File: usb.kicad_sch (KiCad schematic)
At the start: 4 parts, among them J3 TYPE-C-31-M-12

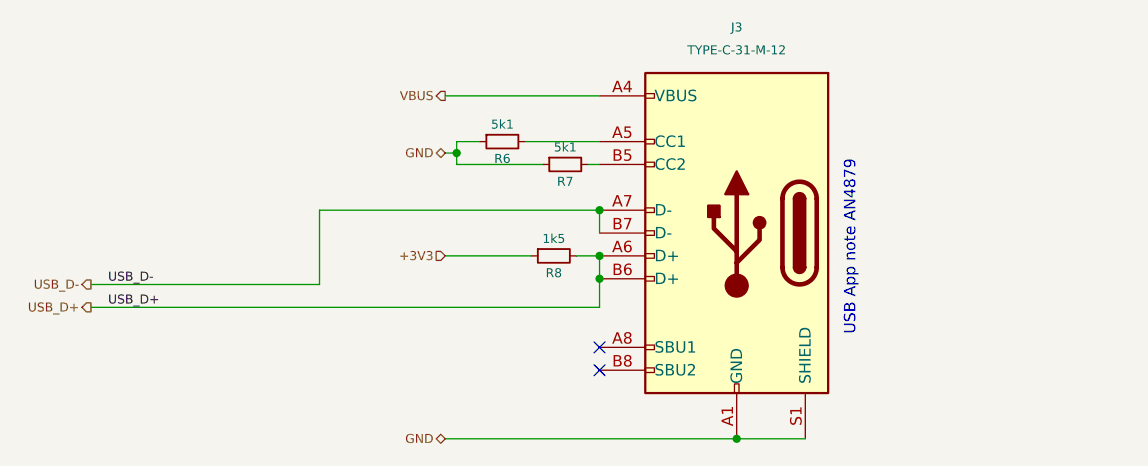
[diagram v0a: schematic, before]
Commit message: Finish schematic with all pins
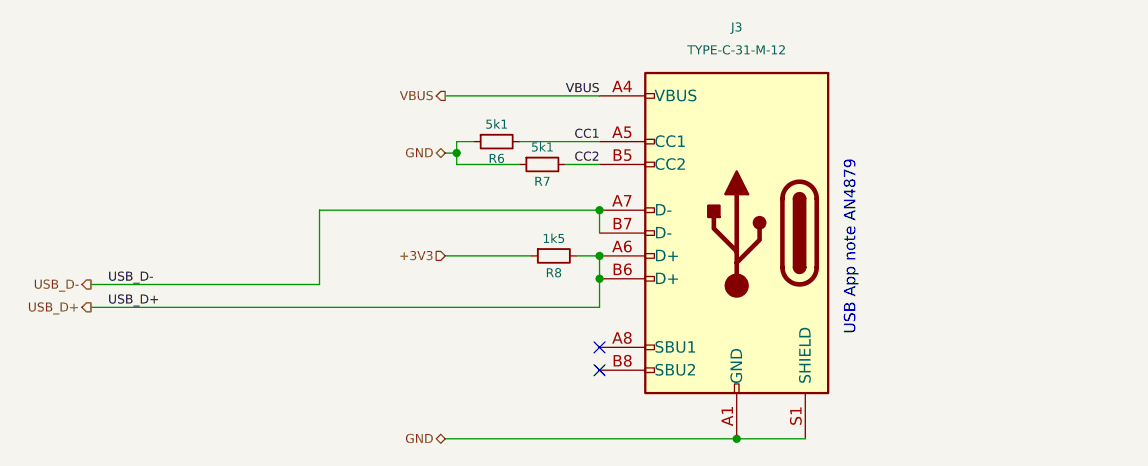
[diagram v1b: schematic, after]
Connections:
- net CC1: now reaches J3.A5 (CC1), R6.2
- net CC2: now reaches J3.B5 (CC2), R7.2
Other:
- moved on the sheet: R6, R7
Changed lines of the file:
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@@
   (no_connect (at 102.235 62.865))
   (no_connect (at 102.235 65.405))
-  (wire (pts (xy 95.885 42.545) (xy 86.36 42.545))
+  (wire (pts (xy 93.345 42.545) (xy 86.36 42.545))
     (stroke (width 0) (type default))
   )
@@
     (stroke (width 0) (type default))
   )
-  (wire (pts (xy 102.235 42.545) (xy 100.965 42.545))
+  (wire (pts (xy 102.235 42.545) (xy 98.425 42.545))
     (stroke (width 0) (type default))
   )
@@
     (stroke (width 0) (type default))
   )
-  (wire (pts (xy 102.235 40.005) (xy 93.98 40.005))
+  (wire (pts (xy 102.235 40.005) (xy 93.345 40.005))
     (stroke (width 0) (type default))
   )
@@
     (stroke (width 0) (type default))
   )
-  (wire (pts (xy 88.9 40.005) (xy 86.36 40.005))
+  (wire (pts (xy 88.265 40.005) (xy 86.36 40.005))
     (stroke (width 0) (type default))
   )
@@
     (effects (font (size 1.27 1.27)) (justify left bottom))
   )
+  (label "VBUS" (at 102.235 34.925 180) (fields_autoplaced)
+    (effects (font (size 1 1)) (justify right bottom))
+  )
   (label "USB_D-" (at 47.625 55.88 0) (fields_autoplaced)
     (effects (font (size 1 1)) (justify left bottom))
@@
     (effects (font (size 1 1)) (justify left bottom))
   )
+  (label "CC2" (at 102.235 42.545 180) (fields_autoplaced)
+    (effects (font (size 1 1)) (justify right bottom))
+  )
+  (label "CC1" (at 102.235 40.005 180) (fields_autoplaced)
+    (effects (font (size 1 1)) (justify right bottom))
+  )
   (hierarchical_label "USB_D-" (shape output) (at 45.72 55.88 180) (fields_autoplaced)
     (effects (font (size 1 1)) (justify right))
@@
     (effects (font (size 1 1)) (justify right))
   )
-  (symbol (lib_id "Device:R_Small") (at 91.44 40.005 90) (mirror x) (unit 1)
+  (symbol (lib_id "Device:R_Small") (at 90.805 40.005 90) (mirror x) (unit 1)
     (in_bom yes) (on_board yes) (dnp no)
-    (property "Reference" "R6" (at 91.44 41.91 90)
-      (effects (font (size 1 1)))
-    )
-    (property "Value" "5k1" (at 91.44 38.1 90)
-      (effects (font (size 1 1)))
-    )
-    (property "Footprint" "Resistor_SMD:R_0402_1005Metric" (at 91.44 40.005 0)
-      (effects (font (size 1 1)) hide)
-    )
-    (property "Datasheet" "~" (at 91.44 40.005 0)
-      (effects (font (size 1 1)) hide)
-    )
-    (property "Description" "62.5mW Thick Film Resistors ±100ppm/℃ ±1% 5.1kΩ 0402  Chip Resistor - Surface Mount ROHS" (at 91.44 40.005 0)
-      (effects (font (size 1 1)) hide)
-    )
-    (property "JLCPCB Part #" "C25905" (at 91.44 40.005 0)
-      (effects (font (size 1 1)) hide)
-    )
-    (property "Manufacturer" "UNI-ROYAL(Uniroyal Elec)" (at 91.44 40.005 0)
-      (effects (font (size 1 1)) hide)
-    )
-    (property "Manufacturer_Part_Number" "0402WGF5101TCE" (at 91.44 40.005 0)
-      (effects (font (size 1 1)) hide)
-    )
-    (property "Partnumber" "0402WGF5101TCE" (at 91.44 40.005 0)
-      (effects (font (size 1 1)) hide)
-    )
-    (property "Manufacturer_Name" "UNI-ROYAL(Uniroyal Elec)" (at 91.44 40.005 0)
-      (effects (font (size 1 1)) hide)
-    )
-    (property "isBasicPart" "YES" (at 91.44 40.005 0)
+    (property "Reference" "R6" (at 90.805 41.91 90)
+      (effects (font (size 1 1)))
+    )
+    (property "Value" "5k1" (at 90.805 38.1 90)
+      (effects (font (size 1 1)))
+    )
+    (property "Footprint" "Resistor_SMD:R_0402_1005Metric" (at 90.805 40.005 0)
+      (effects (font (size 1 1)) hide)
+    )
+    (property "Datasheet" "~" (at 90.805 40.005 0)
+      (effects (font (size 1 1)) hide)
+    )
+    (property "Description" "62.5mW Thick Film Resistors ±100ppm/℃ ±1% 5.1kΩ 0402  Chip Resistor - Surface Mount ROHS" (at 90.805 40.005 0)
+      (effects (font (size 1 1)) hide)
+    )
+    (property "JLCPCB Part #" "C25905" (at 90.805 40.005 0)
+      (effects (font (size 1 1)) hide)
+    )
+    (property "Manufacturer" "UNI-ROYAL(Uniroyal Elec)" (at 90.805 40.005 0)
+      (effects (font (size 1 1)) hide)
+    )
+    (property "Manufacturer_Part_Number" "0402WGF5101TCE" (at 90.805 40.005 0)
+      (effects (font (size 1 1)) hide)
+    )
+    (property "Partnumber" "0402WGF5101TCE" (at 90.805 40.005 0)
+      (effects (font (size 1 1)) hide)
+    )
+    (property "Manufacturer_Name" "UNI-ROYAL(Uniroyal Elec)" (at 90.805 40.005 0)
+      (effects (font (size 1 1)) hide)
+    )
+    (property "isBasicPart" "YES" (at 90.805 40.005 0)
       (effects (font (size 1 1)) hide)
     )
@@
     )
   )
-  (symbol (lib_id "Device:R_Small") (at 98.425 42.545 90) (mirror x) (unit 1)
+  (symbol (lib_id "Device:R_Small") (at 95.885 42.545 90) (mirror x) (unit 1)
     (in_bom yes) (on_board yes) (dnp no)
-    (property "Reference" "R7" (at 98.425 44.45 90)
-      (effects (font (size 1 1)))
-    )
-    (property "Value" "5k1" (at 98.425 40.64 90)
-      (effects (font (size 1 1)))
-    )
-    (property "Footprint" "Resistor_SMD:R_0402_1005Metric" (at 98.425 42.545 0)
-      (effects (font (size 1 1)) hide)
-    )
-    (property "Datasheet" "~" (at 98.425 42.545 0)
-      (effects (font (size 1 1)) hide)
-    )
-    (property "Description" "62.5mW Thick Film Resistors ±100ppm/℃ ±1% 5.1kΩ 0402  Chip Resistor - Surface Mount ROHS" (at 98.425 42.545 0)
-      (effects (font (size 1 1)) hide)
-    )
-    (property "JLCPCB Part #" "C25905" (at 98.425 42.545 0)
-      (effects (font (size 1 1)) hide)
-    )
-    (property "Manufacturer" "UNI-ROYAL(Uniroyal Elec)" (at 98.425 42.545 0)
-      (effects (font (size 1 1)) hide)
-    )
-    (property "Manufacturer_Part_Number" "0402WGF5101TCE" (at 98.425 42.545 0)
-      (effects (font (size 1 1)) hide)
-    )
-    (property "Partnumber" "0402WGF5101TCE" (at 98.425 42.545 0)
-      (effects (font (size 1 1)) hide)
-    )
-    (property "Manufacturer_Name" "UNI-ROYAL(Uniroyal Elec)" (at 98.425 42.545 0)
-      (effects (font (size 1 1)) hide)
-    )
-    (property "isBasicPart" "YES" (at 98.425 42.545 0)
-      (effects (font (size 1 1)) hide)
-    )
+    (property "Reference" "R7" (at 95.885 44.45 90)
+      (effects (font (size 1 1)))
+    )
+    (property "Value" "5k1" (at 95.885 40.64 90)
+      (effects (font (size 1 1)))
+    )
+    (property "Footprint" "Resistor_SMD:R_0402_1005Metric" (at 95.885 42.545 0)
+      (effects (font (size 1 1)) hide)
+    )
+    (property "Datasheet" "~" (at 95.885 42.545 0)
+      (effects (font (size 1 1)) hide)
+    )
+    (property "Description" "62.5mW Thick Film Resistors ±100ppm/℃ ±1% 5.1kΩ 0402  Chip Resistor - Surface Mount ROHS" (at 95.885 42.545 0)
+      (effects (font (size 1 1)) hide)
+    )
+    (property "JLCPCB Part #" "C25905" (at 95.885 42.545 0)
+      (effects (font (size 1 1)) hide)
+    )
+    (property "Manufacturer" "UNI-ROYAL(Uniroyal Elec)" (at 95.885 42.545 0)
+      (effects (font (size 1 1)) hide)
+    )
+    (property "Manufacturer_Part_Number" "0402WGF5101TCE" (at 95.885 42.545 0)
+      (effects (font (size 1 1)) hide)
+    )
+    (property "Partnumber" "0402WGF5101TCE" (at 95.885 42.545 0)
+      (effects (font (size 1 1)) hide)
+    )
+    (property "Manufacturer_Name" "UNI-ROYAL(Uniroyal Elec)" (at 95.885 42.545 0)
+      (effects (font (size 1 1)) hide)
+    )
+    (property "isBasicPart" "YES" (at 95.885 42.545 0)
+      (effects (font (size 1 1)) hide)
+    )

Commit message: WIP
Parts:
- removed J3: TYPE-C-31-M-12, Connector_USB:USB_C_Receptacle_HRO_TYPE-C-31-M-12, symbol Project_Library:USB_C_Receptacle_USB2.0
- added J2: SHOU HAN TYPE-C 16PIN 2MD(073) (C2765186), Project_Library:SHOU HAN TYPE-C 16PIN 2MD(073) (C2765186), symbol Project_Library:SHOU HAN TYPE-C 16PIN 2MD(073) (C2765186)
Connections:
- net CC1: now also J2.A5 (CC1)
- net CC2: now also J2.B5 (CC2)
- net GND: now also J2.A1 (GND), J2.A12 (GND), J2.B1 (GND), J2.B12 (GND), J2.S1 (SHIELD)
- net USB_D+: now also J2.A6 (D+), J2.B6 (D+)
- net USB_D-: now also J2.A7 (D-), J2.B7 (D-)
- net VBUS: now also J2.A4 (VBUS), J2.A9 (VBUS), J2.B4 (VBUS), J2.B9 (VBUS)
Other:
- moved on the sheet: R8

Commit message: #1 Use new central library KiCad-Lib
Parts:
- J2: footprint Project_Library:SHOU HAN TYPE-C 16PIN 2MD(073) (C2765186) -> #Connector:SHOU HAN TYPE-C 16PIN 2MD(073); symbol Project_Library:SHOU HAN TYPE-C 16PIN 2MD(073) (C2765186) -> #Connector:SHOU HAN TYPE-C 16PIN 2MD(073)
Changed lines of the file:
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@@
     (effects (font (size 1 1)) (justify right))
   )
-  (symbol (lib_id "Project_Library:SHOU HAN TYPE-C 16PIN 2MD(073) (C2765186)") (at 117.475 50.165 0) (mirror y) (unit 1)
+  (symbol (lib_id "#Connector:SHOU HAN TYPE-C 16PIN 2MD(073)") (at 117.475 50.165 0) (mirror y) (unit 1)
     (in_bom yes) (on_board yes) (dnp no)
     (property "Reference" "J2" (at 128.905 48.895 0)
@@
       (effects (font (size 1.27 1.27)) (justify right))
     )
-    (property "Footprint" "Project_Library:SHOU HAN TYPE-C 16PIN 2MD(073) (C2765186)" (at 116.967 82.677 0)
+    (property "Footprint" "#Connector:SHOU HAN TYPE-C 16PIN 2MD(073)" (at 116.967 82.677 0)
       (effects (font (size 1.27 1.27)) hide)
     )
-    (property "Datasheet" "https://datasheet.lcsc.com/lcsc/2111231930_SHOU-HAN-TYPE-C-16PIN-2MD-073_C2765186.pdf" (at 118.999 80.391 0)
+    (property "Datasheet" "${KIPRJMOD}/KiCad-Lib/#Connector.doc/SHOU HAN TYPE-C 16PIN 2MD(073).pdf" (at 118.999 80.391 0)
       (effects (font (size 1.27 1.27)) hide)
     )
@@
       (effects (font (size 1.27 1.27)) hide)
     )
-    (property "JLCPCB Part #" "C2765186" (at 117.475 85.725 0)
+    (property "JLCPCB Part #" "C2765186" (at 117.475 85.725 0) (show_name)
       (effects (font (size 1.27 1.27)) hide)
     )
-    (property "isBasicPart" "NO" (at 117.475 95.885 0)
+    (property "isBasicPart" "NO" (at 117.475 95.885 0) (show_name)
       (effects (font (size 1.27 1.27)) hide)
     )

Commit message: WIP
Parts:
- renumbered J2 to J201
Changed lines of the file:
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@@
   (symbol (lib_id "#Connector:SHOU HAN TYPE-C 16PIN 2MD(073)") (at 117.475 50.165 0) (mirror y) (unit 1)
     (in_bom yes) (on_board yes) (dnp no)
-    (property "Reference" "J2" (at 128.905 48.895 0)
-      (effects (font (size 1.27 1.27)) (justify right))
+    (property "Reference" "J201" (at 128.905 48.895 0)
+      (effects (font (size 1 1)) (justify right))
     )
     (property "Value" "SHOU HAN TYPE-C 16PIN 2MD(073) (C2765186)" (at 107.95 30.48 0)
-      (effects (font (size 1.27 1.27)) (justify right))
+      (effects (font (size 1 1)) (justify right))
     )
     (property "Footprint" "#Connector:SHOU HAN TYPE-C 16PIN 2MD(073)" (at 116.967 82.677 0)
@@
       (project "stm32f4_uno"
         (path "/e63e39d7-6ac0-4ffd-8aa3-1841a4541b55/7fb4eaf4-74c6-419d-8578-6cd0a966ea13"
-          (reference "J2") (unit 1)
+          (reference "J201") (unit 1)
         )
       )
@@
         )
         (path "/e63e39d7-6ac0-4ffd-8aa3-1841a4541b55/7fb4eaf4-74c6-419d-8578-6cd0a966ea13"
-          (reference "R401") (unit 1)
+          (reference "R201") (unit 1)
         )
       )
@@
         )
         (path "/e63e39d7-6ac0-4ffd-8aa3-1841a4541b55/7fb4eaf4-74c6-419d-8578-6cd0a966ea13"
-          (reference "R402") (unit 1)
+          (reference "R202") (unit 1)
         )
       )
@@
         )
         (path "/e63e39d7-6ac0-4ffd-8aa3-1841a4541b55/7fb4eaf4-74c6-419d-8578-6cd0a966ea13"
-          (reference "R403") (unit 1)
-        )
-      )
+          (reference "R203") (unit 1)
+        )
+      )

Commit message: #2 Add silkscreen texts
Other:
- company: (none) -> easy-smart solution GmbH
- title: (none) -> STM32F4 Uno
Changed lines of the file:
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@@
 (kicad_sch (version 20230121) (generator eeschema)
   (paper "A4")
+  (title_block
+    (title "STM32F4 Uno")
+    (date "2023-10-02")
+    (rev "1.0.x-dev")
+    (company "easy-smart solution GmbH")
+  )
   (junction (at 74.295 41.275) (diameter 0) (color 0 0 0 0)
   )
